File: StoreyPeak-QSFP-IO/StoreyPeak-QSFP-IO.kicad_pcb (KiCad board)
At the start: 2 copper layers, 30.1 x 69.8 mm, 32 parts, among them U1 QSFP_PCB-QSFP, U3 CH340G, X1 X322512MSB4SI

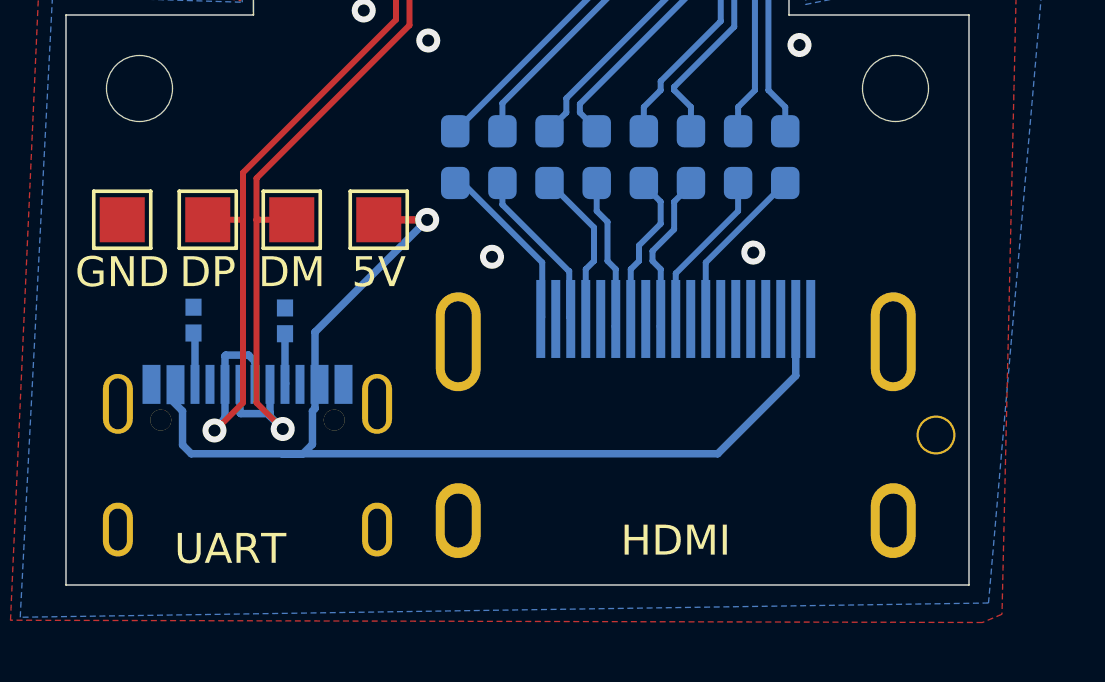
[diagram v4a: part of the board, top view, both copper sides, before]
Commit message: Increase clearance between USB-C port and HDMI port/CC resistors
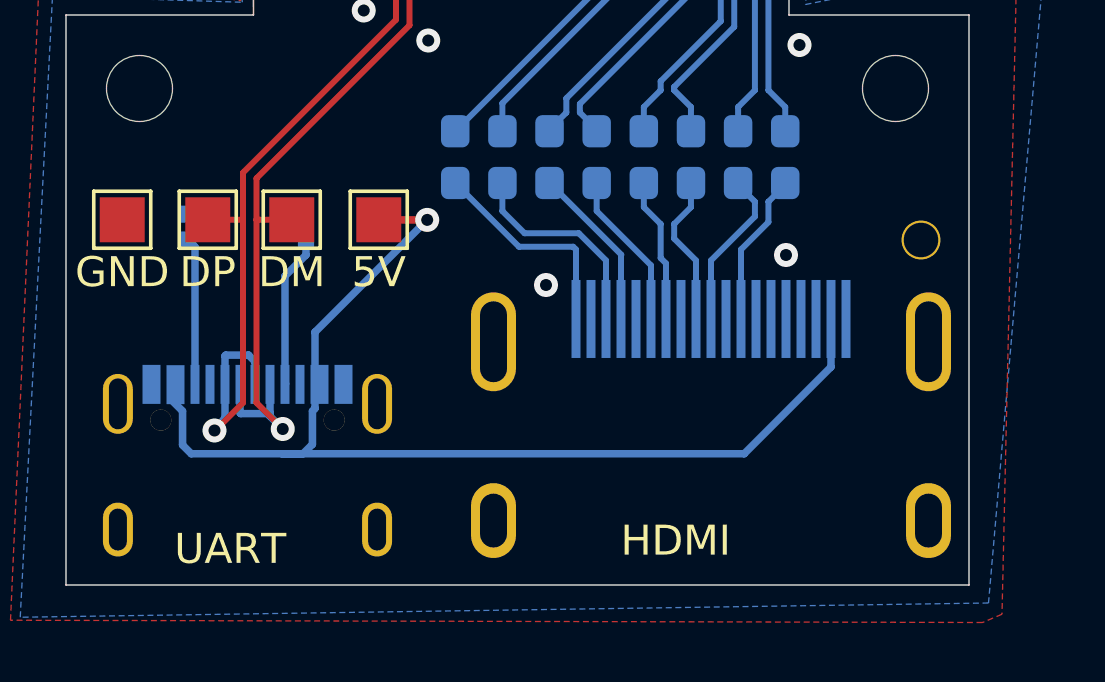
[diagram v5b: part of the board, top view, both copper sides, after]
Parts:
- moved H6 6.52 mm to (175.4, 121.5)
- moved R1 3.20 mm to (154.9, 121.1)
- moved R2 3.11 mm to (151.0, 121.1)
- moved HDMI1 1.18 mm to (168.4, 127.5)
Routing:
- net Net-(USB1-CC1): track 1.72 -> 5.14 mm
- net Net-(USB1-CC2): track 1.73 -> 4.91 mm
- net /HDMI_D2-: track 5.49 -> 7.02 mm
- net +5V: track 37.2 -> 38.5 mm
- net /HDMI_D0+: track 5.83 -> 4.84 mm
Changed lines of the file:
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@@
 	(footprint "MountingHole:JLCPCB_Tooling_Hole"
 		(layer "F.Cu")
-		(at 175.9 128)
+		(at 175.4 121.5)
 		(descr "Mounting Hole 2.1mm, no annular")
 		(tags "mounting hole 2.1mm no annular")
@@
 	(footprint "easyeda2kicad:HDMI-SMD_HD-A-05H9192N"
 		(layer "B.Cu")
-		(at 167.225 127.4925 180)
+		(at 168.4 127.4925 180)
 		(property "Reference" "HDMI1"
 			(at 0.5 0.5175 180)
@@
 	(footprint "easyeda2kicad:R0402"
 		(layer "B.Cu")
-		(at 151.15 124.17 -90)
+		(at 150.97 121.07 -90)
 		(property "Reference" "R2"
 			(at -0.07 1.725 90)
@@
 	(footprint "easyeda2kicad:R0402"
 		(layer "B.Cu")
-		(at 154.2 124.195 -90)
+		(at 154.9 121.07 -90)
 		(property "Reference" "R1"
-			(at -0.145 -1.725 90)
+			(at 0.43 -1.725 90)
 			(layer "B.SilkS")
 			(effects
@@
 	)
 	(via
-		(at 169.81 121.92)
+		(at 170.9 122)
 		(size 0.8)
 		(drill 0.4)
@@
 	)
 	(via
-		(at 161.1 122.06)
+		(at 162.9 123)
 		(size 0.8)
 		(drill 0.4)
@@
 	)
 	(segment
-		(start 168.625 128.625)
-		(end 171.225 126.025)
+		(start 172.4 125.7325)
+		(end 172.4 124.1325)
 		(width 0.25)
 		(layer "B.Cu")
@@
 	)
 	(segment
-		(start 171.225 126.025)
-		(end 171.225 124.425)
-		(width 0.25)
-		(layer "B.Cu")
-		(net 2)
-	)
-	(segment
-		(start 154.1 128.625)
-		(end 168.625 128.625)
+		(start 169.5075 128.625)
+		(end 172.4 125.7325)
 		(width 0.25)
 		(layer "B.Cu")
@@
 	)
 	(segment
-		(start 167.732143 119.6625)
-		(end 167.171429 120.223214)
-		(width 0.2)
-		(layer "B.Cu")
-		(net 3)
-	)
-	(segment
-		(start 167.171429 120.223214)
-		(end 167.171429 121.146771)
-		(width 0.2)
+		(start 154.1 128.625)
+		(end 169.5075 128.625)
+		(width 0.25)
 		(layer "B.Cu")
-		(net 3)
+		(net 2)
 	)
 	(segment
 		(start 167.732143 119.6)
-		(end 167.732143 119.6625)
+		(end 167.732143 120.406251)
 		(width 0.2)
 		(layer "B.Cu")
@@
 	)
 	(segment
-		(start 167.171429 121.146771)
-		(end 166.45 121.8682)
+		(start 167.171429 120.966965)
+		(end 167.171429 121.453229)
 		(width 0.2)
 		(layer "B.Cu")
@@
 	)
 	(segment
-		(start 166.45 122.199999)
-		(end 166.725 122.474999)
+		(start 167.732143 120.406251)
+		(end 167.171429 120.966965)
 		(width 0.2)
 		(layer "B.Cu")
@@
 	)
 	(segment
-		(start 166.45 121.8682)
-		(end 166.45 122.199999)
+		(start 167.9 122.1818)
+		(end 167.9 124.1325)
 		(width 0.2)
 		(layer "B.Cu")
@@
 	)
 	(segment
-		(start 166.725 122.474999)
-		(end 166.725 124.425)
+		(start 167.171429 121.453229)
+		(end 167.9 122.1818)
 		(width 0.2)
 		(layer "B.Cu")
@@
 	)
 	(segment
-		(start 166.675 124.375)
-		(end 166.725 124.425)
-		(width 0.2)
-		(layer "B.Cu")
-		(net 3)
-	)
-	(segment
-		(start 166.721429 120.223214)
-		(end 166.721429 120.960371)
-		(width 0.2)
-		(layer "B.Cu")
-		(net 4)
-	)
-	(segment
-		(start 166 122.199999)
-		(end 165.725 122.474999)
-		(width 0.2)
-		(layer "B.Cu")
-		(net 4)
-	)
-	(segment
-		(start 166 121.6818)
-		(end 166 122.199999)
-		(width 0.2)
-		(layer "B.Cu")
-		(net 4)
-	)
-	(segment
 		(start 166.160715 119.6)
-		(end 166.160715 119.6625)
+		(end 166.160715 120.406251)
 		(width 0.2)
 		(layer "B.Cu")
@@
 	)
 	(segment
-		(start 166.160715 119.6625)
-		(end 166.721429 120.223214)
+		(start 166.721429 122.101487)
+		(end 166.9 122.280058)
 		(width 0.2)
 		(layer "B.Cu")
@@
 	)
 	(segment
-		(start 165.725 122.474999)
-		(end 165.725 124.425)
+		(start 166.721429 120.966965)
+		(end 166.721429 122.101487)
 		(width 0.2)
 		(layer "B.Cu")
@@
 	)
 	(segment
-		(start 165.725 124.061397)
-		(end 165.725 124.425)
+		(start 166.9 122.280058)
+		(end 166.9 124.1325)
 		(width 0.2)
 		(layer "B.Cu")
@@
 	)
 	(segment
-		(start 166.721429 120.960371)
-		(end 166 121.6818)
+		(start 166.160715 120.406251)
+		(end 166.721429 120.966965)
 		(width 0.2)
 		(layer "B.Cu")
@@
 	)
 	(segment
-		(start 165.175 124.375)
-		(end 165.225 124.425)
-		(width 0.2)
-		(layer "B.Cu")
-		(net 5)
-	)
-	(segment
-		(start 164.95 122.199999)
-		(end 164.95 120.895744)
-		(width 0.2)
-		(layer "B.Cu")
-		(net 5)
-	)
-	(segment
-		(start 164.95 120.895744)
+		(start 164.589287 119.6)
 		(end 164.589287 120.535031)
 		(width 0.2)
@@
 	)
 	(segment
-		(start 165.225 122.474999)
-		(end 164.95 122.199999)
-		(width 0.2)
-		(layer "B.Cu")
-		(net 5)
-	)
-	(segment
-		(start 165.225 124.425)
-		(end 165.225 122.474999)
+		(start 166.4 122.345744)
+		(end 166.4 124.1325)
 		(width 0.2)
 		(layer "B.Cu")
@@
 	(segment
 		(start 164.589287 120.535031)
-		(end 164.589287 119.6)
+		(end 166.4 122.345744)
 		(width 0.2)
 		(layer "B.Cu")
@@
 	)
 	(segment
-		(start 164.5 121.082141)
-		(end 163.017859 119.6)
+		(start 165.40893 121.99107)
+		(end 165.4 122)
 		(width 0.2)
 		(layer "B.Cu")
@@
 	)
 	(segment
-		(start 164.225 122.474999)
-		(end 164.5 122.199999)
+		(start 163.017859 119.6)
+		(end 165.40893 121.99107)
 		(width 0.2)
 		(layer "B.Cu")
@@
 	)
 	(segment
-		(start 164.5 122.199999)
-		(end 164.5 121.082141)
+		(start 165.4 122)
+		(end 165.4 124.1325)
 		(width 0.2)
 		(layer "B.Cu")
@@
 	)
 	(segment
-		(start 164.225 124.425)
-		(end 164.225 122.474999)
+		(start 162.1864 121.275)
+		(end 163.9932 121.275)
 		(width 0.2)
 		(layer "B.Cu")
-		(net 6)
+		(net 7)
 	)
 	(segment
-		(start 163.675 124.0825)
-		(end 163.725 124.1325)
+		(start 161.446431 119.6)
+		(end 161.446431 120.535031)
 		(width 0.2)
 		(layer "B.Cu")
@@
 	)
 	(segment
-		(start 161.446431 119.6)
-		(end 161.446431 120.321431)
+		(start 163.9932 121.275)
+		(end 164.9 122.1818)
 		(width 0.2)
 		(layer "B.Cu")
@@
 	)
 	(segment
-		(start 161.446431 120.321431)
-		(end 163.6575 122.5325)
+		(start 164.9 122.1818)
+		(end 164.9 124.1325)
 		(width 0.2)
 		(layer "B.Cu")
@@
 	)
 	(segment
-		(start 163.675 122.5325)
-		(end 163.675 124.0825)
+		(start 161.446431 120.535031)
+		(end 162.1864 121.275)
 		(width 0.2)
 		(layer "B.Cu")
@@
 	)
 	(segment
-		(start 163.6575 122.5325)
-		(end 163.675 122.5325)
+		(start 159.875003 119.6)
+		(end 162.000003 121.725)
 		(width 0.2)
 		(layer "B.Cu")
-		(net 7)
+		(net 8)
 	)
 	(segment
-		(start 162.725 124.425)
-		(end 162.725 123.275)
+		(start 163.9 121.8182)
+		(end 163.9 124.1325)
 		(width 0.2)
 		(layer "B.Cu")
@@
 	)
 	(segment
-		(start 162.775 122.25)
-		(end 162.775 124.0825)
+		(start 163.8068 121.725)
+		(end 163.9 121.8182)
 		(width 0.2)
 		(layer "B.Cu")
@@
 	)
 	(segment
-		(start 159.875003 119.6)
-		(end 160.125 119.6)
+		(start 162.000003 121.725)
+		(end 163.8068 121.725)
 		(width 0.2)
 		(layer "B.Cu")
@@
 	)
 	(segment
-		(start 162.775 124.0825)
-		(end 162.725 124.1325)
+		(start 170.314285 120.903915)
+		(end 170.314285 120.223215)
 		(width 0.2)
 		(layer "B.Cu")
-		(net 8)
+		(net 9)
 	)
 	(segment
-		(start 160.125 119.6)
-		(end 162.775 122.25)
+		(start 170.314285 120.223215)
+		(end 170.875 119.6625)
 		(width 0.2)
 		(layer "B.Cu")
-		(net 8)
+		(net 9)
+	)
+	(segment
+		(start 170.875 119.6625)
+		(end 170.875 119.6)
+		(width 0.2)
+		(layer "B.Cu")
+		(net 9)
 	)
 	(segment
-		(start 170.875 119.6)
-		(end 168.225 122.25)
+		(start 169.4 124.1325)
+		(end 169.4 121.8182)
 		(width 0.2)
 		(layer "B.Cu")
@@
 	)
 	(segment
-		(start 168.225 122.25)
-		(end 168.225 124.1325)
+		(start 169.4 121.8182)
+		(end 170.314285 120.903915)
 		(width 0.2)
 		(layer "B.Cu")
@@
 	)
 	(segment
+		(start 169.864286 120.223215)
+		(end 169.864286 120.717514)
+		(width 0.2)
+		(layer "B.Cu")
+		(net 10)
+	)
+	(segment
 		(start 169.303571 119.6)
-		(end 169.303571 120.535032)
+		(end 169.303571 119.6625)
+		(width 0.2)
+		(layer "B.Cu")
+		(net 10)
+	)
+	(segment
+		(start 168.4 122.1818)
+		(end 168.4 124.1325)
 		(width 0.2)
 		(layer "B.Cu")
@@
 	)
 	(segment
-		(start 169.303571 120.535032)
-		(end 167.225 122.613603)
+		(start 169.864286 120.717514)
+		(end 168.4 122.1818)
 		(width 0.2)
 		(layer "B.Cu")
@@
 	)
 	(segment
-		(start 167.225 122.613603)
-		(end 167.225 124.1325)
+		(start 169.303571 119.6625)
+		(end 169.864286 120.223215)
 		(width 0.2)
 		(layer "B.Cu")
@@
 	)
 	(segment
-		(start 154.2 124.625)
+		(start 154.2 122.7)
 		(end 154.2 126.3125)
 		(width 0.25)
@@
 	)
 	(segment
-		(start 151.15 124.6)
-		(end 151.2 124.65)
+		(start 154.9 122)
+		(end 154.2 122.7)
+		(width 0.25)
+		(layer "B.Cu")
+		(net 43)
+	)
+	(segment
+		(start 154.9 121.5)
+		(end 154.9 122)
+		(width 0.25)
+		(layer "B.Cu")
+		(net 43)
+	)
+	(segment
+		(start 150.97 121.5)
+		(end 151.2 121.73)
 		(width 0.25)
 		(layer "B.Cu")
@@
 	)
 	(segment
-		(start 151.2 124.65)
+		(start 151.2 121.73)
 		(end 151.2 126.3125)
 		(width 0.25)
